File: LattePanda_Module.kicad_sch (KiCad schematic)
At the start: 10 parts, among them J78 Conn_01x03_Pin

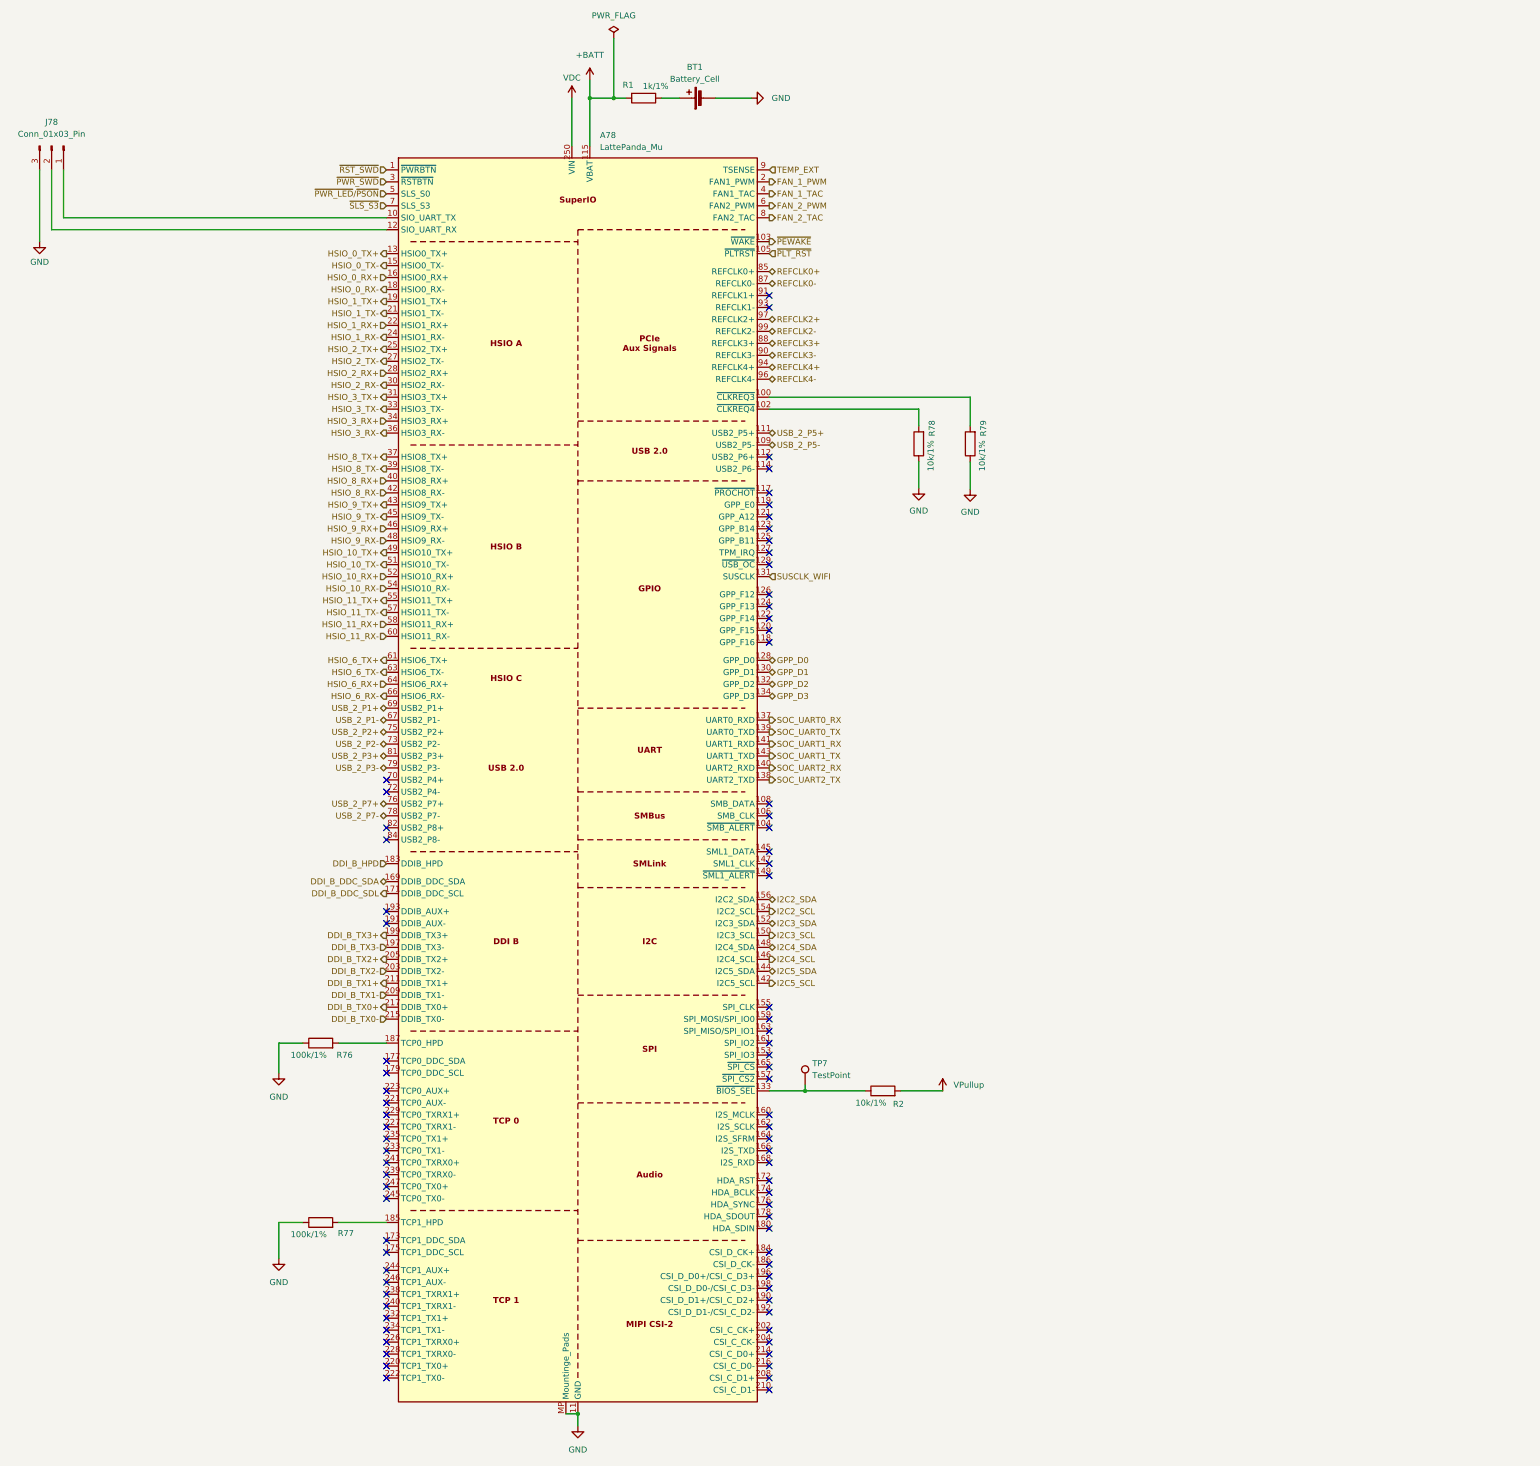
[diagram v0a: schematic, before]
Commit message: Updated all the footprints into the pcb editor but all the designator numbers have changed... I have tp go back and fix each one
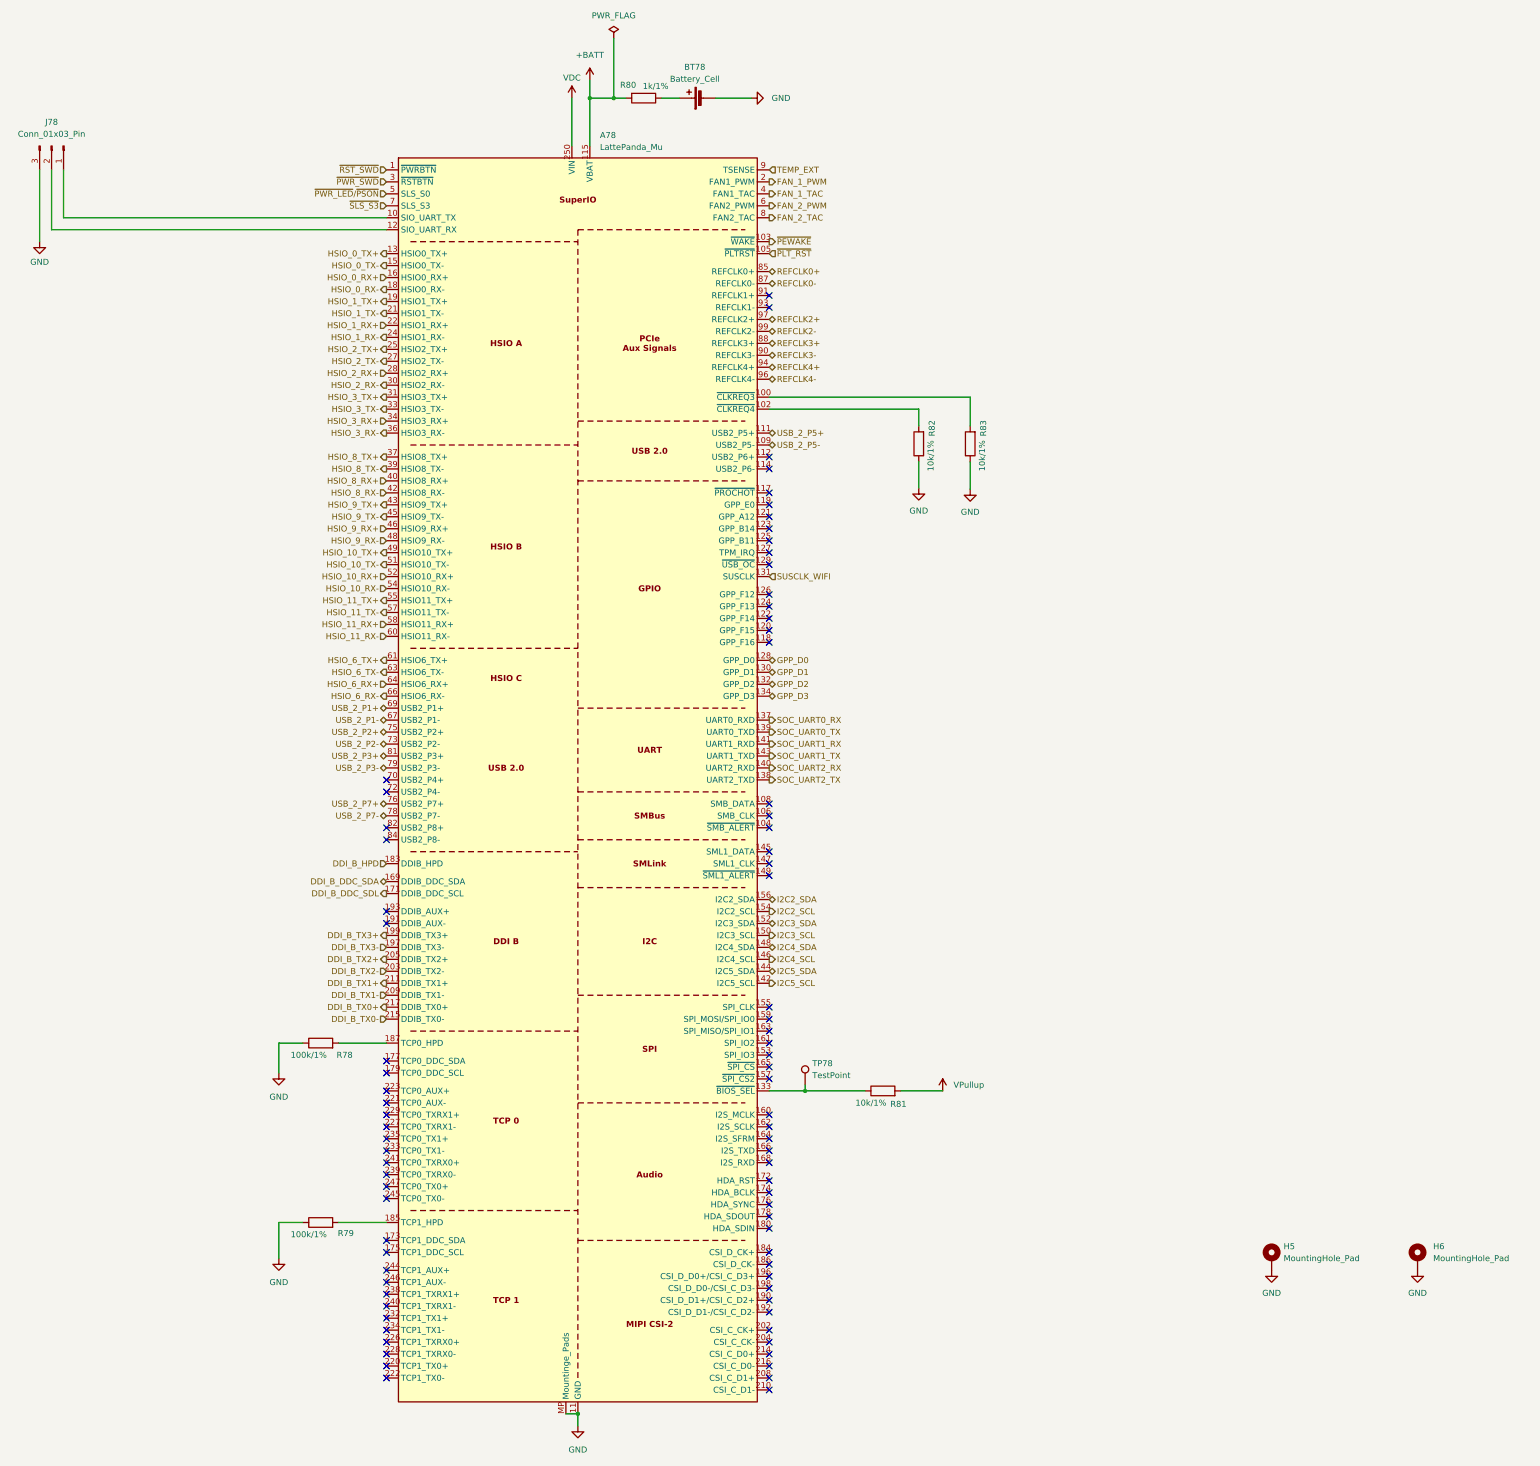
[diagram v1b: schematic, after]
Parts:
- added H5: MountingHole_Pad, A_HDJ_Library:MountingHole_3mm_M2_Pad_TopOnly, symbol Mechanical:MountingHole_Pad
- added H6: MountingHole_Pad, A_HDJ_Library:MountingHole_3.2mm_M3_Pad_Via, symbol Mechanical:MountingHole_Pad
- BT78: renamed from BT1; footprint (none) -> A_HDJ_Library:Battery_Holder_CR1220_S8411-45R
- R78: renamed from R76; footprint (none) -> A_HDJ_Library:R_0402_1005Metric
- R79: renamed from R77; footprint (none) -> A_HDJ_Library:R_0402_1005Metric
- R80: renamed from R1; footprint (none) -> A_HDJ_Library:R_0402_1005Metric
- R81: renamed from R2; footprint (none) -> A_HDJ_Library:R_0402_1005Metric
- R82: renamed from R78; footprint (none) -> A_HDJ_Library:R_0402_1005Metric
- R83: renamed from R79; footprint (none) -> A_HDJ_Library:R_0402_1005Metric
- TP78: renamed from TP7; footprint (none) -> A_HDJ_Library:TestPoint_Pad_D1.5mm
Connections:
- net GND: now also H5.1, H6.1
